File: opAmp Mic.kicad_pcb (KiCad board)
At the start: 2 copper layers, 19 x 80.5 mm, 24 parts, among them J1 XLR3, U1 OPA2134

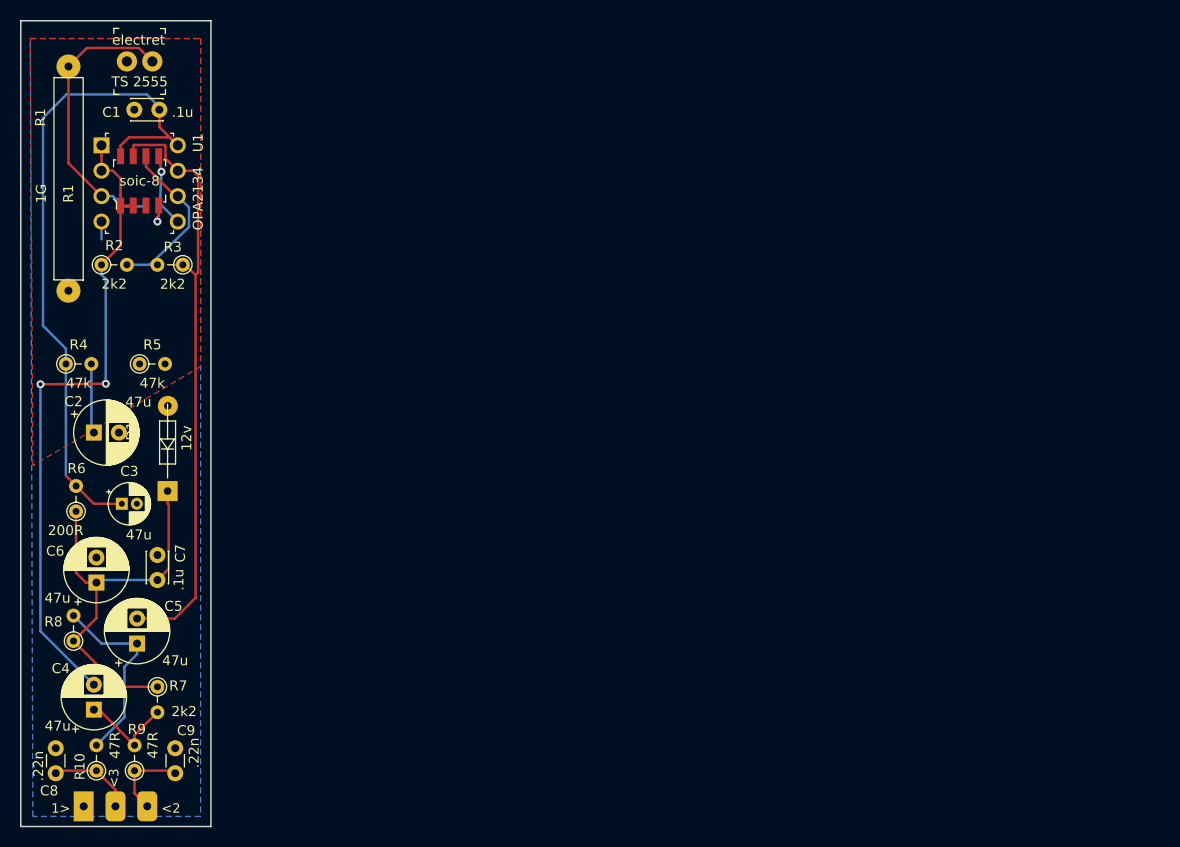
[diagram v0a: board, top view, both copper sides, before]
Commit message: added notes describing what was wrong with the original order from JLC PCB with 2 bodes, I got it working, but there are some issues with part placement that also need fixing
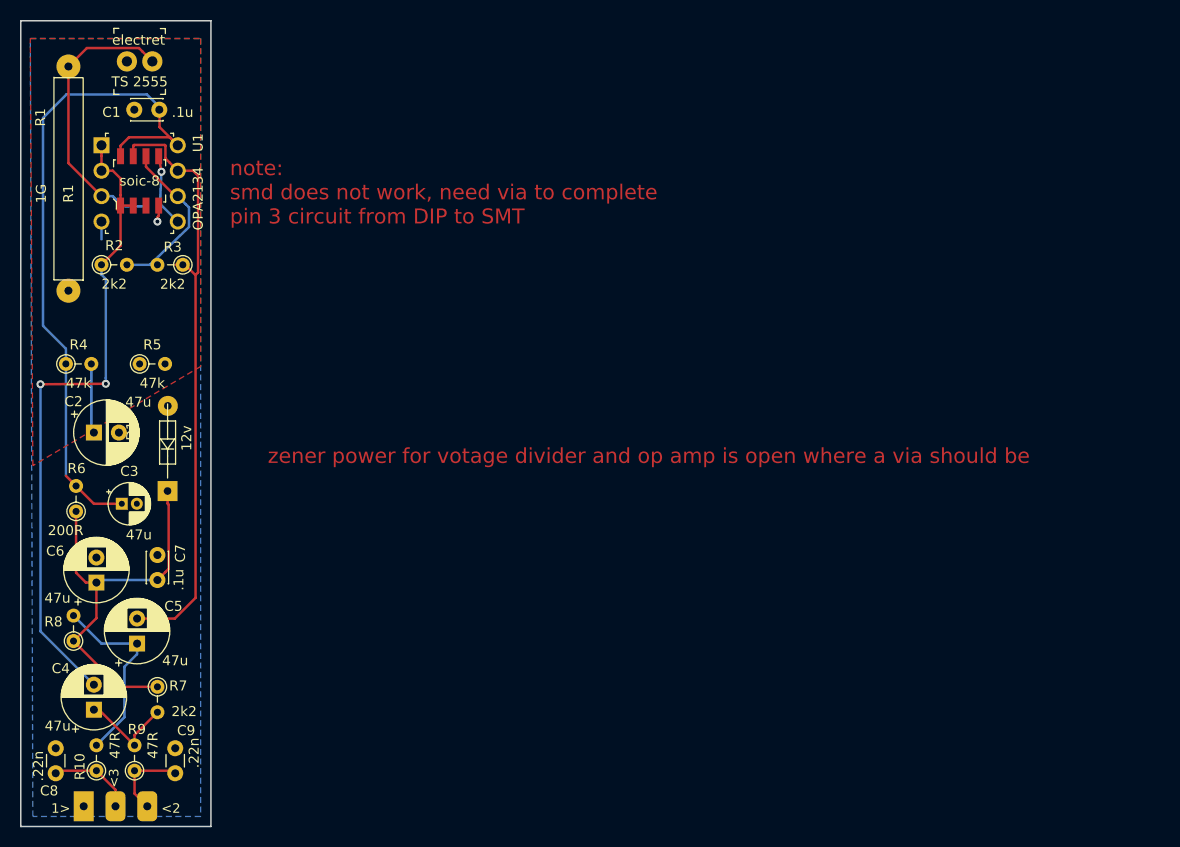
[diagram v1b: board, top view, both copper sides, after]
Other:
- board text added: "note: smd does not work, need via to complete pin 3 circuit from DIP to SMT"
- board text added: "zener power for votage divider and op amp is open where a via should be"
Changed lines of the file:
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@@
   (general
     (thickness 1.6)
-    (drawings 11)
+    (drawings 13)
     (tracks 117)
     (zones 0)
@@
     (solder_mask_min_width 0.25)
     (aux_axis_origin 0 0)
-    (visible_elements FFFFFF7F)
+    (visible_elements 7FFFFFFF)
     (pcbplotparams
       (layerselection 0x010fc_ffffffff)
@@
     )
   )
+  (gr_text "zener power for votage divider and op amp is open where a via should be" (at 172.2882 103.4288) (layer F.Cu)
+    (effects (font (size 1.5 1.5) (thickness 0.3)))
+  )
+  (gr_text "note:\nsmd does not work, need via to complete \npin 3 circuit from DIP to SMT" (at 130.429 77.089) (layer F.Cu)
+    (effects (font (size 1.5 1.5) (thickness 0.3)) (justify left))
+  )
   (gr_text "Electret-> OpAmp\nmicrophone platform" (at 125.984 117.9576 90) (layer B.SilkS)

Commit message: lined up capacitors in the center line remade nets after moving everything
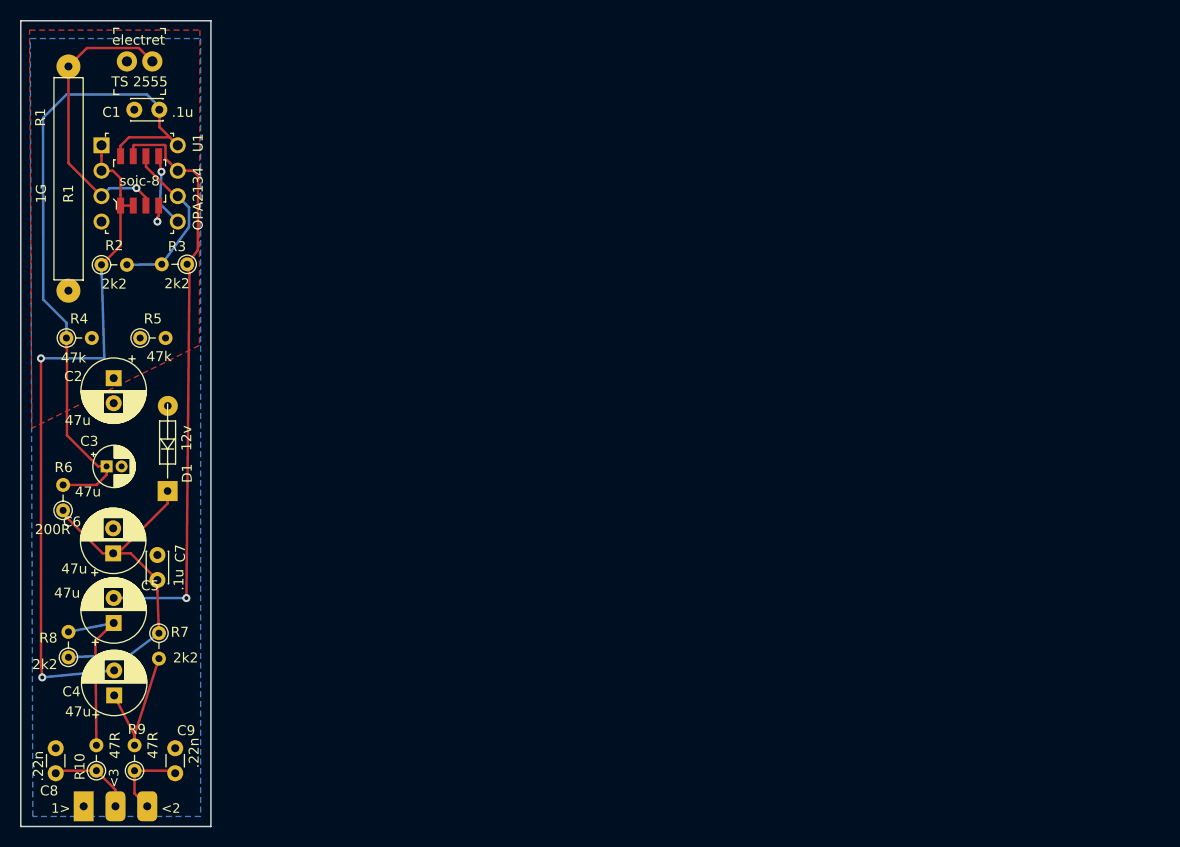
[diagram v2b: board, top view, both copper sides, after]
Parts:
- moved C2 5.79 mm to (118.8, 95.7), turned to 270 degrees
- moved R7 5.36 mm to (123.3, 121.1)
- moved C3 4.03 mm to (118.1, 104.5)
- moved C6 3.37 mm to (118.8, 113.2)
- moved C5 3.11 mm to (118.8, 120.1)
- moved R4 2.59 mm to (114.1, 91.6)
- moved R5 2.59 mm to (121.5, 91.6)
- moved C4 2.48 mm to (118.9, 127.4)
- moved R8 1.70 mm to (114.3, 123.5)
- moved R6 1.30 mm to (113.8, 108.9)
- moved R3 0.43 mm to (126.2, 84.3)
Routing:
- net GND: track 14.5 -> 7.53 mm
- net Net-(C4-Pad2): track 67.1 -> 72.0 mm
- net Net-(C6-Pad1): track 41.2 -> 36.3 mm
- net Net-(C4-Pad1): track 9.79 -> 14.5 mm
- net Earth: track 3.43 -> 1.65 mm
- net Net-(C5-Pad1): track 19.4 -> 17.6 mm
- net Net-(C5-Pad2): track 61.0 -> 59.4 mm, vias 0 -> 1
- net Net-(MK1-Pad2): track 29.5 -> 30.0 mm, vias 0 -> 1
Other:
- board text removed: "note: smd does not work, need via to complete pin 3 circuit from DIP to SMT"
- board text removed: "zener power for votage divider and op amp is open where a via should be"

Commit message: ready for release and board spin
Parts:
- U1: value OPA2134 -> OPA1642
- moved C8 4.69 mm to (113.8, 130.5)
- moved C9 4.68 mm to (124.4, 130.5)
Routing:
- net Net-(C8-Pad1): track 8.51 -> 10.7 mm
- net Net-(C9-Pad1): track 8.25 -> 9.94 mm
- net Net-(C4-Pad2): track 72.0 -> 70.4 mm, vias 2 -> 3
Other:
- outline, holes or cut-outs redrawn
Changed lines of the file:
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@@
   (general
     (thickness 1.6)
-    (drawings 13)
-    (tracks 112)
+    (drawings 17)
+    (tracks 115)
     (zones 0)
     (modules 24)
@@
   )
   (module Capacitor_THT:C_Disc_D3.0mm_W1.6mm_P2.50mm (layer F.Cu)
-    (at 113.03 135.128 90)
+    (at 113.8174 130.5052 90)
     (descr "C, Disc series, Radial, pin pitch=2.50mm, , diameter*width=3.0*1.6mm^2, Capacitor, http://www.vishay.com/docs/45233/krseries.pdf")
     (tags "C Disc series Radial pin pitch 2.50mm  diameter 3.0mm width 1.6mm Capacitor")
-    (fp_text reference C8 (at -1.7526 -0.6604 180) (layer F.SilkS)
-      (effects (font (size 1 1) (thickness 0.15)))
-    )
-    (fp_text value .22n (at 0.7112 -1.7272 90) (layer F.SilkS)
+    (fp_text reference C8 (at -0.1778 -2.1844 270) (layer F.SilkS)
+      (effects (font (size 1 1) (thickness 0.15)))
+    )
+    (fp_text value .22n (at -2.0574 -0.7112 180) (layer F.SilkS)
       (effects (font (size 1 1) (thickness 0.15)))
     )
@@
   )
   (module Capacitor_THT:C_Disc_D3.0mm_W1.6mm_P2.50mm (layer F.Cu)
-    (at 124.968 135.128 90)
+    (at 124.4346 130.4798 90)
     (descr "C, Disc series, Radial, pin pitch=2.50mm, , diameter*width=3.0*1.6mm^2, Capacitor, http://www.vishay.com/docs/45233/krseries.pdf")
     (tags "C Disc series Radial pin pitch 2.50mm  diameter 3.0mm width 1.6mm Capacitor")
-    (fp_text reference C9 (at 4.2672 1.0922 180) (layer F.SilkS)
-      (effects (font (size 1 1) (thickness 0.15)))
-    )
-    (fp_text value .22n (at 2.032 1.8796 90) (layer F.SilkS)
+    (fp_text reference C9 (at -0.0254 2.032 270) (layer F.SilkS)
+      (effects (font (size 1 1) (thickness 0.15)))
+    )
+    (fp_text value .22n (at -2.032 0.6858 180) (layer F.SilkS)
       (effects (font (size 1 1) (thickness 0.15)))
     )
@@
     (descr "Resistor, Axial_DIN0204 series, Axial, Vertical, pin pitch=2.54mm, 0.167W, length*diameter=3.6*1.6mm^2, http://cdn-reichelt.de/documents/datenblatt/B400/1_4W%23YAG.pdf")
     (tags "Resistor Axial_DIN0204 series Axial Vertical pin pitch 2.54mm 0.167W length 3.6mm diameter 1.6mm")
-    (fp_text reference R10 (at 0.4064 -1.651 90) (layer F.SilkS)
+    (fp_text reference R10 (at 2.159 -1.778 90) (layer F.SilkS)
       (effects (font (size 1 1) (thickness 0.15)))
     )
@@
     (fp_line (start 3.49 1.05) (end 3.49 -1.05) (layer F.CrtYd) (width 0.05))
     (fp_line (start 3.49 -1.05) (end -1.05 -1.05) (layer F.CrtYd) (width 0.05))
-    (fp_text user %R (at 0.4318 -1.6256 90) (layer F.Fab)
+    (fp_text user %R (at 2.1336 -1.7526 90) (layer F.Fab)
       (effects (font (size 1 1) (thickness 0.15)))
     )
@@
     (at 117.602 72.39)
     (descr http://media.digikey.com/pdf/Data%20Sheets/Lite-On%20PDFs/6N137%20Series.pdf)
-    (fp_text reference U1 (at 9.652 -0.254 90) (layer F.SilkS)
-      (effects (font (size 1 1) (thickness 0.15)))
-    )
-    (fp_text value OPA2134 (at 9.652 5.334 90) (layer F.SilkS)
+    (fp_text reference U1 (at 0.0508 -2.1844 180) (layer F.SilkS)
+      (effects (font (size 1 1) (thickness 0.15)))
+    )
+    (fp_text value OPA1642 (at 9.652 5.334 90) (layer F.SilkS)
       (effects (font (size 1 1) (thickness 0.15)))
     )
@@
     (descr "CP, Radial series, Radial, pin pitch=2.50mm, , diameter=6.3mm, Electrolytic Capacitor")
     (tags "CP Radial series Radial pin pitch 2.50mm  diameter 6.3mm Electrolytic Capacitor")
-    (fp_text reference C4 (at 0.381 -4.2672 180) (layer F.SilkS)
-      (effects (font (size 1 1) (thickness 0.15)))
-    )
-    (fp_text value 47u (at -1.6256 -3.6068 180) (layer F.SilkS)
+    (fp_text reference C4 (at -1.905 -2.9972 180) (layer F.SilkS)
+      (effects (font (size 1 1) (thickness 0.15)))
+    )
+    (fp_text value 47u (at -2.9972 -1.778 180) (layer F.SilkS)
       (effects (font (size 1 1) (thickness 0.15)))
     )
@@
     )
   )
-  (gr_text 1> (at 113.5106 139.1686) (layer B.SilkS)
+  (gr_line (start 113.7666 140.462) (end 124.2822 140.462) (layer Edge.Cuts) (width 0.15))
+  (gr_line (start 124.2822 133.35) (end 124.2822 140.462) (layer Edge.Cuts) (width 0.15))
+  (gr_line (start 128.5117 133.35) (end 124.2822 133.35) (layer Edge.Cuts) (width 0.15))
+  (gr_line (start 113.7666 133.4008) (end 109.5502 133.4008) (layer Edge.Cuts) (width 0.15))
+  (gr_text 1> (at 114.6556 135.2804 270) (layer B.SilkS)
     (effects (font (size 0.95 0.95) (thickness 0.1)) (justify bottom))
   )
-  (gr_text <2 (at 124.536 139.194) (layer B.SilkS)
+  (gr_text <2 (at 123.5202 135.3312 90) (layer B.SilkS)
     (effects (font (size 0.95 0.95) (thickness 0.1)) (justify bottom))
   )
@@
     (effects (font (size 0.95 0.95) (thickness 0.1)) (justify bottom mirror))
   )
-  (gr_text <2 (at 124.536 139.194) (layer F.SilkS)
+  (gr_text <2 (at 123.4186 135.3566 90) (layer F.SilkS)
     (effects (font (size 0.95 0.95) (thickness 0.1)) (justify bottom))
   )
@@
     (effects (font (size 0.95 0.95) (thickness 0.1)) (justify bottom))
   )
-  (gr_text 1> (at 113.536 139.194) (layer F.SilkS)
+  (gr_text 1> (at 114.5794 135.2804 270) (layer F.SilkS)
     (effects (font (size 0.95 0.95) (thickness 0.1)) (justify bottom))
   )
   (gr_line (start 109.5371 59.9476) (end 128.5371 59.9476) (layer Edge.Cuts) (width 0.15))
-  (gr_line (start 128.5371 59.9476) (end 128.5371 140.4476) (layer Edge.Cuts) (width 0.15))
-  (gr_line (start 109.5371 140.4476) (end 109.5371 59.9476) (layer Edge.Cuts) (width 0.15))
-  (gr_line (start 128.536 140.4476) (end 109.5371 140.4476) (layer Edge.Cuts) (width 0.15))
+  (gr_line (start 128.5371 59.9476) (end 128.5371 133.35) (layer Edge.Cuts) (width 0.15))
+  (gr_line (start 109.5502 133.4008) (end 109.5371 59.9476) (layer Edge.Cuts) (width 0.15))
+  (gr_line (start 113.7666 133.4008) (end 113.7666 140.4476) (layer Edge.Cuts) (width 0.15))
   (segment (start 120.347999 71.590001) (end 124.422001 71.590001) (width 0.25) (layer F.Cu) (net 1))
   (segment (start 124.422001 71.590001) (end 125.222 72.39) (width 0.25) (layer F.Cu) (net 1))
@@
   (segment (start 117.602 73.44) (end 117.602 74.93) (width 0.25) (layer F.Cu) (net 4))
   (segment (start 117.602 72.39) (end 117.602 73.44) (width 0.25) (layer F.Cu) (net 4))
-  (via (at 111.5568 93.6752) (size 0.8) (drill 0.4) (layers F.Cu B.Cu) (net 4))
   (segment (start 119.507 82.423) (end 117.602 84.328) (width 0.25) (layer F.Cu) (net 4))
   (segment (start 119.507 78.411) (end 119.507 82.423) (width 0.25) (layer F.Cu) (net 4))
   (segment (start 117.348 84.328) (end 117.602 84.328) (width 0.25) (layer B.Cu) (net 4))
-  (segment (start 117.602 84.328) (end 117.602 85.317949) (width 0.25) (layer B.Cu) (net 4))
-  (segment (start 117.8814 93.6752) (end 111.5568 93.6752) (width 0.25) (layer B.Cu) (net 4))
-  (segment (start 117.602 84.328) (end 117.8814 93.6752) (width 0.25) (layer B.Cu) (net 4))
-  (segment (start 111.5568 124.1552) (end 111.5568 93.6752) (width 0.25) (layer F.Cu) (net 4))
   (via (at 111.6838 125.5522) (size 0.8) (drill 0.4) (layers F.Cu B.Cu) (net 4))
-  (segment (start 111.6838 125.5522) (end 111.5568 124.1552) (width 0.25) (layer F.Cu) (net 4))
   (segment (start 111.6838 125.5522) (end 118.872 124.8556) (width 0.25) (layer B.Cu) (net 4))
+  (via (at 112.8776 93.6244) (size 0.8) (drill 0.4) (layers F.Cu B.Cu) (net 4))
+  (segment (start 111.5568 124.1552) (end 111.6838 125.5522) (width 0.25) (layer F.Cu) (net 4))
+  (segment (start 112.8776 93.6244) (end 111.5568 124.1552) (width 0.25) (layer F.Cu) (net 4))
+  (segment (start 118.604487 85.330487) (end 117.602 84.328) (width 0.25) (layer F.Cu) (net 4))
+  (segment (start 119.0752 92.5322) (end 118.604487 85.330487) (width 0.25) (layer F.Cu) (net 4))
+  (via (at 119.0752 92.5322) (size 0.8) (drill 0.4) (layers F.Cu B.Cu) (net 4))
+  (segment (start 112.8776 93.6244) (end 119.0752 92.5322) (width 0.25) (layer B.Cu) (net 4))
   (segment (start 120.904 131.318) (end 123.3424 123.6726) (width 0.25) (layer F.Cu) (net 5))
   (segment (start 120.904 132.334) (end 120.904 131.318) (width 0.25) (layer F.Cu) (net 5))
@@
   (segment (start 118.999 136.779) (end 117.094 134.874) (width 0.25) (layer F.Cu) (net 9))
   (segment (start 118.999 138.43) (end 118.999 136.779) (width 0.25) (layer F.Cu) (net 9))
-  (segment (start 113.284 134.874) (end 113.03 135.128) (width 0.25) (layer F.Cu) (net 9))
-  (segment (start 117.094 134.874) (end 113.284 134.874) (width 0.25) (layer F.Cu) (net 9))
+  (segment (start 113.8174 132.587349) (end 113.8174 131.63657) (width 0.25) (layer F.Cu) (net 9))
+  (segment (start 116.104051 134.874) (end 113.8174 132.587349) (width 0.25) (layer F.Cu) (net 9))
+  (segment (start 113.8174 131.63657) (end 113.8174 130.5052) (width 0.25) (layer F.Cu) (net 9))
+  (segment (start 117.094 134.874) (end 116.104051 134.874) (width 0.25) (layer F.Cu) (net 9))
   (segment (start 120.904 137.16) (end 120.904 134.874) (width 0.25) (layer F.Cu) (net 10))
   (segment (start 122.174 138.43) (end 120.904 137.16) (width 0.25) (layer F.Cu) (net 10))
-  (segment (start 124.714 134.874) (end 124.968 135.128) (width 0.25) (layer F.Cu) (net 10))
-  (segment (start 120.904 134.874) (end 124.714 134.874) (width 0.25) (layer F.Cu) (net 10))
+  (segment (start 124.4346 131.3434) (end 124.4346 130.4798) (width 0.25) (layer F.Cu) (net 10))
+  (segment (start 120.904 134.874) (end 124.4346 131.3434) (width 0.25) (layer F.Cu) (net 10))
   (segment (start 118.401999 76.670001) (end 121.094399 76.670001) (width 0.25) (layer B.Cu) (net 11))
   (segment (start 117.602 77.47) (end 118.401999 76.670001) (width 0.25) (layer B.Cu) (net 11))
@@
     (polygon
       (pts
-        (xy 127.508 139.446) (xy 110.744 139.446) (xy 110.49 61.722) (xy 127.508 61.722)
+        (xy 127.508 132.334) (xy 123.7996 132.4102) (xy 123.825 139.446) (xy 119.126 139.446) (xy 114.0206 139.446)
+        (xy 114.0714 132.334) (xy 110.72026 132.181429) (xy 110.49 61.722) (xy 127.508 61.722)
       )
     )
